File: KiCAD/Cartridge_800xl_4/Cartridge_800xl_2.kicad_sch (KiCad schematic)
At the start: 21 parts, among them SW1 Reset, U1 27C512, U2 74HC165, U3 74HC595, U4 GAL16V8, U5 TXS0108EPW, U6 mini_esp32

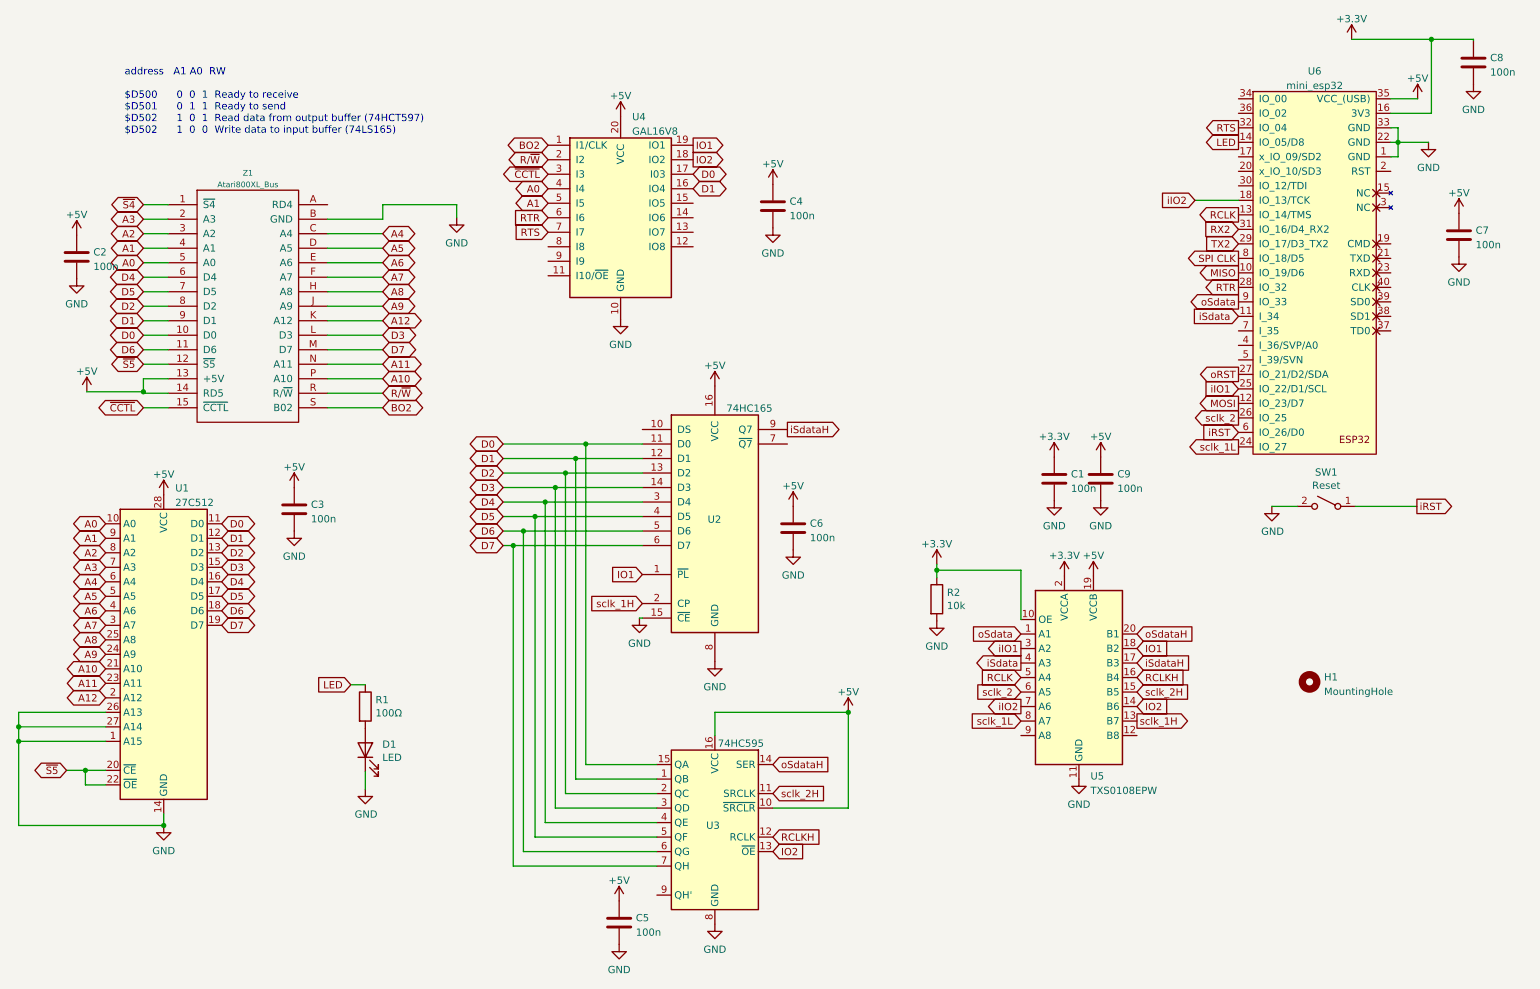
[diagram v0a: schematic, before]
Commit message: version 3
No more sub version in file name
Fixed the userlist issue
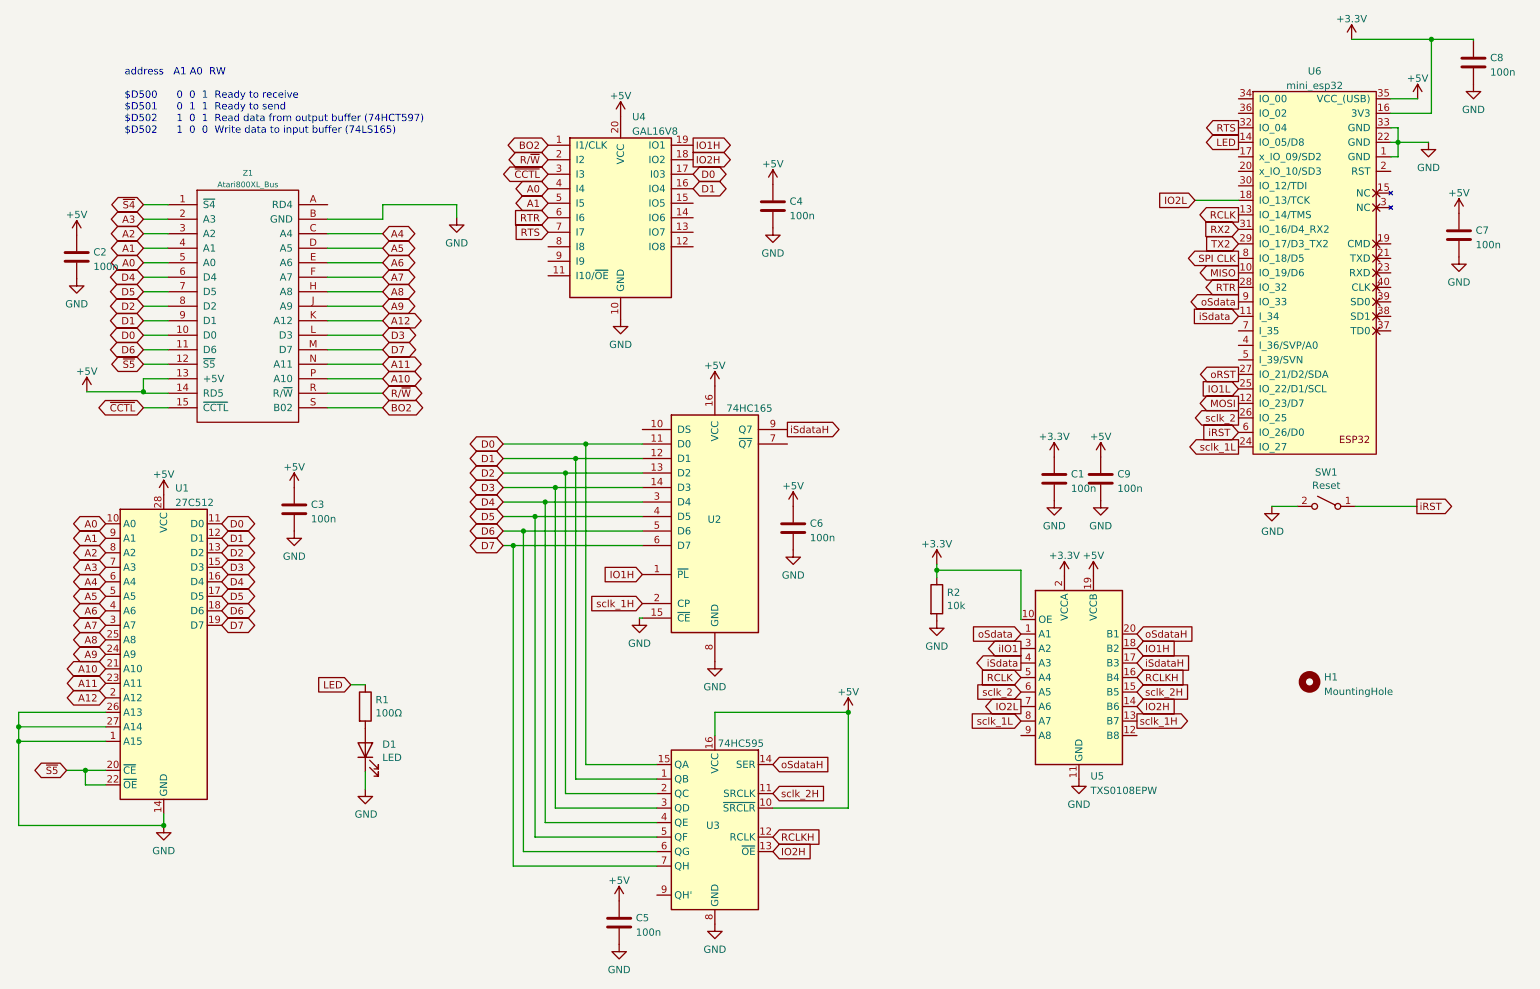
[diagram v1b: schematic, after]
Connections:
- net iIO1: no longer U6.25 (IO_22/D1/SCL)
- net IO1 renamed IO1H
- net IO2 renamed IO2H
- net iIO2 renamed IO2L
- new net IO1L: U6.25 (IO_22/D1/SCL)
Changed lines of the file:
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@@
     )
   )
-  (global_label "IO1" (shape output) (at 139.446 45.72 0) (fields_autoplaced)
-    (effects (font (size 1.27 1.27)) (justify left))
-    (property "Intersheet References" "${INTERSHEET_REFS}" (id 0) (at 145.0039 45.6406 0)
+  (global_label "IO1H" (shape output) (at 139.446 45.72 0) (fields_autoplaced)
+    (effects (font (size 1.27 1.27)) (justify left))
+    (property "Intersheet References" "${INTERSHEET_REFS}" (id 0) (at 146.3343 45.6406 0)
       (effects (font (size 1.27 1.27)) (justify left) hide)
     )
@@
     )
   )
-  (global_label "iIO2" (shape output) (at 196.85 144.018 180) (fields_autoplaced)
-    (effects (font (size 1.27 1.27)) (justify right))
-    (property "Intersheet References" "${INTERSHEET_REFS}" (id 0) (at 190.6874 144.0974 0)
+  (global_label "IO2L" (shape output) (at 196.85 144.018 180) (fields_autoplaced)
+    (effects (font (size 1.27 1.27)) (justify right))
+    (property "Intersheet References" "${INTERSHEET_REFS}" (id 0) (at 190.264 143.9386 0)
       (effects (font (size 1.27 1.27)) (justify right) hide)
     )
@@
     )
   )
-  (global_label "IO2" (shape output) (at 139.446 48.26 0) (fields_autoplaced)
-    (effects (font (size 1.27 1.27)) (justify left))
-    (property "Intersheet References" "${INTERSHEET_REFS}" (id 0) (at 145.0039 48.1806 0)
-      (effects (font (size 1.27 1.27)) (justify left) hide)
-    )
-  )
-  (global_label "IO1" (shape input) (at 130.556 120.904 180) (fields_autoplaced)
-    (effects (font (size 1.27 1.27)) (justify right))
-    (property "Intersheet References" "${INTERSHEET_REFS}" (id 0) (at 124.9981 120.8246 0)
-      (effects (font (size 1.27 1.27)) (justify right) hide)
-    )
-  )
-  (global_label "IO2" (shape input) (at 217.17 144.018 0) (fields_autoplaced)
-    (effects (font (size 1.27 1.27)) (justify left))
-    (property "Intersheet References" "${INTERSHEET_REFS}" (id 0) (at 222.7279 144.0974 0)
+  (global_label "IO2H" (shape output) (at 139.446 48.26 0) (fields_autoplaced)
+    (effects (font (size 1.27 1.27)) (justify left))
+    (property "Intersheet References" "${INTERSHEET_REFS}" (id 0) (at 146.3343 48.1806 0)
+      (effects (font (size 1.27 1.27)) (justify left) hide)
+    )
+  )
+  (global_label "IO1H" (shape input) (at 130.556 120.904 180) (fields_autoplaced)
+    (effects (font (size 1.27 1.27)) (justify right))
+    (property "Intersheet References" "${INTERSHEET_REFS}" (id 0) (at 123.6677 120.8246 0)
+      (effects (font (size 1.27 1.27)) (justify right) hide)
+    )
+  )
+  (global_label "IO2H" (shape input) (at 217.17 144.018 0) (fields_autoplaced)
+    (effects (font (size 1.27 1.27)) (justify left))
+    (property "Intersheet References" "${INTERSHEET_REFS}" (id 0) (at 224.0583 143.9386 0)
       (effects (font (size 1.27 1.27)) (justify left) hide)
     )
@@
     )
   )
-  (global_label "iIO1" (shape input) (at 234.95 88.392 180) (fields_autoplaced)
-    (effects (font (size 1.27 1.27)) (justify right))
-    (property "Intersheet References" "${INTERSHEET_REFS}" (id 0) (at 228.7874 88.3126 0)
+  (global_label "IO1L" (shape input) (at 234.95 88.392 180) (fields_autoplaced)
+    (effects (font (size 1.27 1.27)) (justify right))
+    (property "Intersheet References" "${INTERSHEET_REFS}" (id 0) (at 228.364 88.3126 0)
       (effects (font (size 1.27 1.27)) (justify right) hide)
     )
@@
     )
   )
-  (global_label "iIO2" (shape input) (at 227.33 55.372 180) (fields_autoplaced)
-    (effects (font (size 1.27 1.27)) (justify right))
-    (property "Intersheet References" "${INTERSHEET_REFS}" (id 0) (at 221.1674 55.2926 0)
+  (global_label "IO2L" (shape input) (at 227.33 55.372 180) (fields_autoplaced)
+    (effects (font (size 1.27 1.27)) (justify right))
+    (property "Intersheet References" "${INTERSHEET_REFS}" (id 0) (at 220.744 55.2926 0)
       (effects (font (size 1.27 1.27)) (justify right) hide)
     )
@@
     )
   )
-  (global_label "IO1" (shape input) (at 217.17 133.858 0) (fields_autoplaced)
-    (effects (font (size 1.27 1.27)) (justify left))
-    (property "Intersheet References" "${INTERSHEET_REFS}" (id 0) (at 222.7279 133.9374 0)
+  (global_label "IO1H" (shape input) (at 217.17 133.858 0) (fields_autoplaced)
+    (effects (font (size 1.27 1.27)) (justify left))
+    (property "Intersheet References" "${INTERSHEET_REFS}" (id 0) (at 224.0583 133.7786 0)
       (effects (font (size 1.27 1.27)) (justify left) hide)
     )
@@
     )
   )
-  (global_label "IO2" (shape input) (at 153.416 169.418 0) (fields_autoplaced)
-    (effects (font (size 1.27 1.27)) (justify left))
-    (property "Intersheet References" "${INTERSHEET_REFS}" (id 0) (at 158.9739 169.4974 0)
-      (effects (font (size 1.27 1.27)) (justify left) hide)
-    )
+  (global_label "IO2H" (shape input) (at 153.416 169.418 0) (fields_autoplaced)
+    (effects (font (size 1.27 1.27)) (justify left))
+    (property "Intersheet References" "${INTERSHEET_REFS}" (id 0) (at 160.3043 169.3386 0)
+      (effects (font (size 1.27 1.27)) (justify left) hide)
+    )

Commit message: pcb update
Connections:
- net iIO1 is gone; now on net IO1L: U5.3 (A2)

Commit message: pcb update
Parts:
- C1, C3, C4, C5, C6, C7, C8, C9: value 100n -> 100nF
- D1: value LED -> LED red
- R2: value 10k -> 10kΩ
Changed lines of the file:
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@@
 (kicad_sch
-	(version 20231120)
+	(version 20250114)
 	(generator "eeschema")
-	(generator_version "8.0")
+	(generator_version "9.0")
 	(paper "A4")
+	(text "address   A1 A0  RW\n\n$D500      0  0  1  Ready to receive\n$D501      0  1  1  Ready to send\n$D502      1  0  1  Read data from output buffer (74HCT597)\n$D502      1  0  0  Write data to input buffer (74LS165)\n"
+		(exclude_from_sim no)
+		(at 39.878 43.942 0)
+		(effects
+			(font
+				(size 1.27 1.27)
+			)
+			(justify left bottom)
+		)
+	)
 	(junction
 		(at 46.736 164.846)
@@
 		)
 	)
-	(text "address   A1 A0  RW\n\n$D500      0  0  1  Ready to receive\n$D501      0  1  1  Ready to send\n$D502      1  0  1  Read data from output buffer (74HCT597)\n$D502      1  0  0  Write data to input buffer (74LS165)\n"
-		(exclude_from_sim no)
-		(at 39.878 43.942 0)
-		(effects
-			(font
-				(size 1.27 1.27)
-			)
-			(justify left bottom)
-		)
-	)
 	(global_label "A6"
 		(shape bidirectional)
@@
 		(fields_autoplaced yes)
 		(property "Reference" "C1"
-			(at 205.613 103.3053 0)
+			(at 205.613 102.9278 0)
 			(effects
 				(font
@@
 			)
 		)
-		(property "Value" "100n"
-			(at 205.613 105.8422 0)
+		(property "Value" "100nF"
+			(at 205.613 105.3521 0)
 			(effects
 				(font
@@
 		(fields_autoplaced yes)
 		(property "Reference" "C7"
-			(at 276.479 60.6333 0)
+			(at 276.479 60.2558 0)
 			(effects
 				(font
@@
 			)
 		)
-		(property "Value" "100n"
-			(at 276.479 63.1702 0)
+		(property "Value" "100nF"
+			(at 276.479 62.6801 0)
 			(effects
 				(font
@@
 			)
 		)
-		(property "Value" "10k"
+		(property "Value" "10kΩ"
 			(at 183.896 126.365 0)
 			(effects
@@
 		(fields_autoplaced yes)
 		(property "Reference" "C4"
-			(at 156.337 55.5533 0)
+			(at 156.337 55.1758 0)
 			(effects
 				(font
@@
 			)
 		)
-		(property "Value" "100n"
-			(at 156.337 58.0902 0)
+		(property "Value" "100nF"
+			(at 156.337 57.6001 0)
 			(effects
 				(font
@@
 		(fields_autoplaced yes)
 		(property "Reference" "C5"
-			(at 129.413 181.0293 0)
+			(at 129.413 180.6518 0)
 			(effects
 				(font
@@
 			)
 		)
-		(property "Value" "100n"
-			(at 129.413 183.5662 0)
+		(property "Value" "100nF"
+			(at 129.413 183.0761 0)
 			(effects
 				(font
@@
 		(fields_autoplaced yes)
 		(property "Reference" "C6"
-			(at 159.893 111.9413 0)
+			(at 159.893 111.5638 0)
 			(effects
 				(font
@@
 			)
 		)
-		(property "Value" "100n"
-			(at 159.893 114.4782 0)
+		(property "Value" "100nF"
+			(at 159.893 113.9881 0)
 			(effects
 				(font
@@
 		(fields_autoplaced yes)
 		(property "Reference" "C3"
-			(at 72.517 108.6393 0)
+			(at 72.517 108.2618 0)
 			(effects
 				(font
@@
 			)
 		)
-		(property "Value" "100n"
-			(at 72.517 111.1762 0)
+		(property "Value" "100nF"
+			(at 72.517 110.6861 0)
 			(effects
 				(font
@@
 		(fields_autoplaced yes)
 		(property "Reference" "C8"
-			(at 279.019 30.4073 0)
+			(at 279.019 30.0298 0)
 			(effects
 				(font
@@
 			)
 		)
-		(property "Value" "100n"
-			(at 279.019 32.9442 0)
+		(property "Value" "100nF"
+			(at 279.019 32.4541 0)
 			(effects
 				(font
@@
 			)
 		)
-		(property "Value" "LED"
+		(property "Value" "LED red"
 			(at 85.0138 152.9588 90)
 			(effects
@@
 		(fields_autoplaced yes)
 		(property "Reference" "C9"
-			(at 213.741 103.3053 0)
+			(at 213.741 102.9278 0)
 			(effects
 				(font
@@
 			)
 		)
-		(property "Value" "100n"
-			(at 213.741 105.8422 0)
+		(property "Value" "100nF"
+			(at 213.741 105.3521 0)
 			(effects
 				(font
@@
 		)
 	)
+	(embedded_fonts no)
 )
